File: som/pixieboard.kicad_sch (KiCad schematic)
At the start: 24 parts, among them J1 Conn_02x20_Counter_Clockwise, J2 Conn_02x20_Counter_Clockwise, J3 Conn_02x20_Counter_Clockwise, J4 Conn_02x20_Counter_Clockwise, J5 Conn_02x20_Counter_Clockwise, J6 Conn_02x20_Counter_Clockwise, J7 Conn_02x20_Counter_Clockwise, U1 XC7A200T-3FBG484E

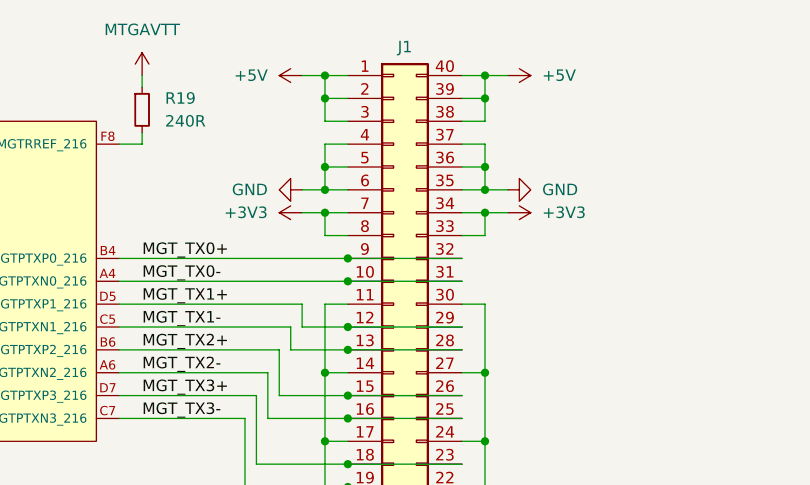
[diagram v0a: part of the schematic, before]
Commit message: Make power traces on SOM thicker, more experimentallingification with carrier I/O layout
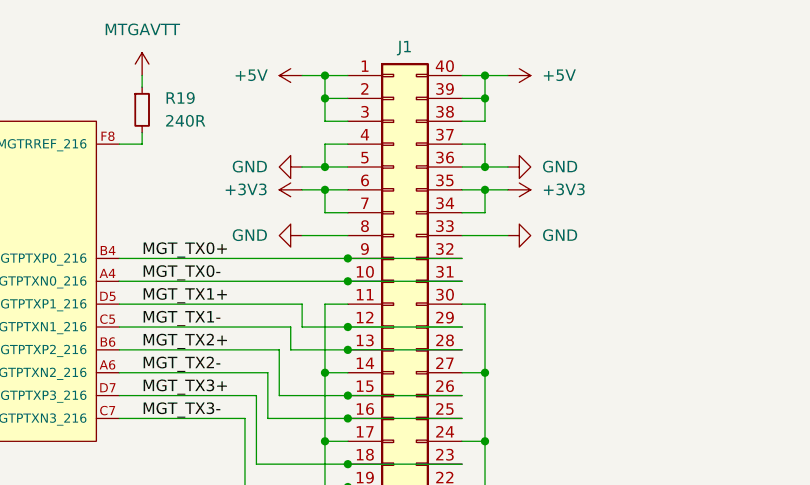
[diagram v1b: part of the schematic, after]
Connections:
- net +3V3: now also J1.35 (Pin_35), J1.6 (Pin_6); no longer J1.33 (Pin_33), J1.8 (Pin_8)
- net GND: now also J1.33 (Pin_33), J1.8 (Pin_8); no longer J1.35 (Pin_35), J1.6 (Pin_6)
